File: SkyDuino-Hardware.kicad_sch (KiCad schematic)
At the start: 45 parts, among them J1 24V, J2 BT, J4 Drum, J5 Exhaust, J6 Cooling, J7 Cooling, J8 NTC, K1 RT314A24, Q1 DMN6075S, Q2 DMN6075S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

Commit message: Add Config field and exclude TH components from assembly
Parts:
- ACL1, ACN1, C1, C5, HEAT1, HEAT2, J1, J4, J5, J6, J7, K1, U6: Config (none) -> -jlcpcb
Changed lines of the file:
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@@
 			)
 		)
+		(property "Config" "-jlcpcb"
+			(at 20.32 77.47 0)
+			(effects
+				(font
+					(size 1.27 1.27)
+				)
+				(hide yes)
+			)
+		)
 		(pin "1"
 		)
@@
 			)
 		)
+		(property "Config" "-jlcpcb"
+			(at 227.33 68.58 0)
+			(effects
+				(font
+					(size 1.27 1.27)
+				)
+				(hide yes)
+			)
+		)
 		(pin "2"
 		)
@@
 			)
 		)
+		(property "Config" "-jlcpcb"
+			(at 245.11 93.98 0)
+			(effects
+				(font
+					(size 1.27 1.27)
+				)
+				(hide yes)
+			)
+		)
 		(pin "12"
 		)
@@
 			)
 		)
+		(property "Config" "-jlcpcb"
+			(at 274.32 86.36 0)
+			(effects
+				(font
+					(size 1.27 1.27)
+				)
+				(hide yes)
+			)
+		)
 		(pin "1"
 		)
@@
 			)
 		)
+		(property "Config" "-jlcpcb"
+			(at 64.77 77.47 0)
+			(effects
+				(font
+					(size 1.27 1.27)
+				)
+				(hide yes)
+			)
+		)
 		(pin "1"
 		)
@@
 			)
 		)
+		(property "Config" "-jlcpcb"
+			(at 274.32 71.12 0)
+			(effects
+				(font
+					(size 1.27 1.27)
+				)
+				(hide yes)
+			)
+		)
 		(pin "1"
 		)
@@
 			)
 		)
+		(property "Config" "-jlcpcb"
+			(at 274.32 66.04 0)
+			(effects
+				(font
+					(size 1.27 1.27)
+				)
+				(hide yes)
+			)
+		)
 		(pin "1"
 		)
@@
 			)
 		)
+		(property "Config" "-jlcpcb"
+			(at 24.13 27.94 0)
+			(effects
+				(font
+					(size 1.27 1.27)
+				)
+				(hide yes)
+			)
+		)
 		(pin "3"
 		)
@@
 			)
 		)
+		(property "Config" "-jlcpcb"
+			(at 36.83 77.47 0)
+			(effects
+				(font
+					(size 1.27 1.27)
+				)
+				(hide yes)
+			)
+		)
 		(pin "1"
 		)
@@
 			)
 		)
+		(property "Config" "-jlcpcb"
+			(at 52.07 77.47 0)
+			(effects
+				(font
+					(size 1.27 1.27)
+				)
+				(hide yes)
+			)
+		)
 		(pin "1"
 		)
@@
 			)
 		)
+		(property "Config" "-jlcpcb"
+			(at 45.72 30.48 0)
+			(effects
+				(font
+					(size 1.27 1.27)
+				)
+				(hide yes)
+			)
+		)
 		(pin "2"
 		)
@@
 			)
 		)
+		(property "Config" "-jlcpcb"
+			(at 121.92 41.91 0)
+			(effects
+				(font
+					(size 1.27 1.27)
+				)
+				(hide yes)
+			)
+		)
 		(pin "2"
 		)
@@
 			(at 274.32 81.28 0)
 			(effects
+				(font
+					(size 1.27 1.27)
+				)
+				(hide yes)
+			)
+		)
+		(property "Config" "-jlcpcb"
+			(at 274.32 81.28 0)
+			(effects

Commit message: Update LCSC field
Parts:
- C2, C9: LCSC (none) -> C377773
- C3, C6, C8: LCSC (none) -> C49678
- C4: LCSC (none) -> C45783
- C7: LCSC (none) -> C1710
- D1, D2, D4: LCSC (none) -> C14996
- J2, J8: Config (none) -> -jlcpcb
- L1: LCSC (none) -> C19947604; LCSC Orig Part (none) -> C19947604
- Q1, Q2, Q3: LCSC (none) -> C155242
- R1: LCSC (none) -> C706252
- R10, R21, R22, R5, R7, R8: LCSC (none) -> C17414
- R2: LCSC (none) -> C17560
- R20, R4, R6: LCSC (none) -> C17408
- R3: LCSC (none) -> C17633
- U1: LCSC (none) -> C5219371; Mouser pn 595-LV3842XFDBVR -> (none)
- U2: LCSC (none) -> C843273
- U3: LCSC (none) -> C52028
- U5: LCSC (none) -> C75864
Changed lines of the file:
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@@
 			)
 		)
-		(property "LCSC" ""
+		(property "LCSC" "C17414"
 			(at 96.52 182.88 0)
 			(effects
@@
 			)
 		)
-		(property "LCSC" ""
+		(property "LCSC" "C75864"
 			(at 36.83 104.14 0)
 			(effects
@@
 			)
 		)
-		(property "LCSC" ""
+		(property "LCSC" "C17408"
 			(at 102.87 134.62 0)
 			(effects
@@
 			)
 		)
-		(property "LCSC" ""
+		(property "LCSC" "C17414"
 			(at 209.55 72.39 0)
 			(effects
@@
 			)
 		)
-		(property "LCSC" ""
+		(property "LCSC" "C706252"
 			(at 100.33 35.56 0)
 			(effects
@@
 			)
 		)
-		(property "LCSC" ""
+		(property "LCSC" "C49678"
 			(at 82.55 27.94 0)
 			(effects
@@
 			)
 		)
-		(property "LCSC" ""
+		(property "LCSC" "C17560"
 			(at 100.33 45.72 0)
 			(effects
@@
 			)
 		)
-		(property "LCSC" ""
+		(property "LCSC" "C14996"
 			(at 86.36 166.37 0)
 			(effects
@@
 			)
 		)
-		(property "LCSC" ""
+		(property "LCSC" "C5219371"
 			(at 68.58 30.48 0)
 			(effects
@@
 			)
 		)
-		(property "Mouser pn" "595-LV3842XFDBVR"
+		(property "Mouser pn" ""
 			(at 68.58 29.21 0)
 			(effects
@@
 			)
 		)
-		(property "LCSC" ""
+		(property "LCSC" "C17633"
 			(at 24.13 115.57 0)
 			(effects
@@
 			)
 		)
-		(property "LCSC" ""
+		(property "LCSC" "C1710"
 			(at 220.98 36.83 0)
 			(effects
@@
 			)
 		)
-		(property "LCSC" ""
+		(property "LCSC" "C17414"
 			(at 96.52 97.79 0)
 			(effects
@@
 			)
 		)
-		(property "LCSC" ""
+		(property "LCSC" "C17408"
 			(at 102.87 179.07 0)
 			(effects
@@
 			)
 		)
-		(property "LCSC" ""
+		(property "LCSC" "C14996"
 			(at 86.36 121.92 0)
 			(effects
@@
 			)
 		)
-		(property "LCSC" ""
+		(property "LCSC" "C49678"
 			(at 265.43 29.21 0)
 			(effects
@@
 			)
 		)
-		(property "LCSC" ""
+		(property "LCSC" "C17414"
 			(at 52.07 110.49 0)
 			(effects
@@
 			)
 		)
+		(property "Config" "-jlcpcb"
+			(at 212.09 35.56 0)
+			(effects
+				(font
+					(size 1.27 1.27)
+				)
+				(hide yes)
+			)
+		)
 		(pin "1"
 		)
@@
 			)
 		)
-		(property "LCSC" ""
+		(property "LCSC" "C377773"
 			(at 52.07 30.48 0)
 			(effects
@@
 			)
 		)
-		(property "LCSC" ""
+		(property "LCSC" "C17414"
 			(at 96.52 138.43 0)
 			(effects
@@
 			)
 		)
-		(property "LCSC" ""
+		(property "LCSC" "C14996"
 			(at 86.36 81.28 0)
 			(effects
@@
 			)
 		)
+		(property "Config" "-jlcpcb"
+			(at 38.1 180.34 0)
+			(effects
+				(font
+					(size 1.27 1.27)
+				)
+				(hide yes)
+			)
+		)
 		(pin "1"
 		)
@@
 			)
 		)
-		(property "LCSC" ""
+		(property "LCSC" "C19947604"
 			(at 93.98 30.48 0)
 			(effects
@@
 			)
 		)
+		(property "Config" ""
+			(at 93.98 30.48 0)
+			(effects
+				(font
+					(size 1.27 1.27)
+				)
+				(hide yes)
+			)
+		)
+		(property "LCSC Orig Part" "C19947604"
+			(at 93.98 30.48 90)
+			(effects
+				(font
+					(size 1.27 1.27)
+				)
+				(hide yes)
+			)
+		)
 		(pin "2"
 		)
@@
 			)
 		)
-		(property "LCSC" ""
+		(property "LCSC" "C377773"
 			(at 64.77 96.52 0)
 			(effects
@@
 			)
 		)
-		(property "LCSC" ""
+		(property "LCSC" "C52028"
 			(at 240.03 36.83 0)
 			(effects
@@
 			)
 		)
-		(property "LCSC" ""
+		(property "LCSC" "C155242"
 			(at 88.9 134.62 0)
 			(effects
@@
 			)
 		)
-		(property "LCSC" ""
+		(property "LCSC" "C155242"
 			(at 88.9 93.98 0)
 			(effects
@@
 			)
 		)
-		(property "LCSC" ""
+		(property "LCSC" "C17414"
 			(at 27.94 173.99 0)
 			(effects
@@
 			)
 		)
-		(property "LCSC" ""
+		(property "LCSC" "C45783"
 			(at 110.49 41.91 0)
 			(effects
@@
 			)
 		)
-		(property "LCSC" ""
+		(property "LCSC" "C49678"
 			(at 179.07 41.91 0)
 			(effects
@@
 			)
 		)
-		(property "LCSC" ""
+		(property "LCSC" "C17408"
 			(at 102.87 93.98 0)
 			(effects
@@
 			)
 		)
-		(property "LCSC" ""
+		(property "LCSC" "C155242"
 			(at 88.9 179.07 0)
 			(effects
@@
 			)
 		)
-		(property "LCSC" ""
+		(property "LCSC" "C843273"
 			(at 161.29 33.02 0)
 			(effects

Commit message: Add JLC rotation offsets
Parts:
- U1: JLCRotOffset (none) -> -90
- U2: JLCRotOffset (none) -> 180
- U5: JLCRotOffset (none) -> 90
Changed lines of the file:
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@@
 			)
 		)
+		(property "Config" ""
+			(at 36.83 104.14 0)
+			(effects
+				(font
+					(size 1.27 1.27)
+				)
+				(hide yes)
+			)
+		)
+		(property "JLCRotOffset" "90"
+			(at 36.83 104.14 0)
+			(effects
+				(font
+					(size 1.27 1.27)
+				)
+				(hide yes)
+			)
+		)
 		(pin "4"
 		)
@@
 			)
 		)
-		(property "Mouser pn" ""
-			(at 68.58 29.21 0)
+		(property "Config" ""
+			(at 68.58 30.48 0)
+			(effects
+				(font
+					(size 1.27 1.27)
+				)
+				(hide yes)
+			)
+		)
+		(property "JLCRotOffset" "-90"
+			(at 68.58 30.48 0)
 			(effects
 				(font
@@
 			(at 161.29 33.02 0)
 			(effects
+				(font
+					(size 1.27 1.27)
+				)
+				(hide yes)
+			)
+		)
+		(property "Config" ""
+			(at 161.29 33.02 0)
+			(effects
+				(font
+					(size 1.27 1.27)
+				)
+				(hide yes)
+			)
+		)
+		(property "JLCRotOffset" "180"
+			(at 161.29 33.02 0)
+			(effects

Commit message: Rotate U5 in correct direction
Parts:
- U5: JLCRotOffset 90 -> -90
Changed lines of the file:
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@@
 			)
 		)
-		(property "JLCRotOffset" "90"
+		(property "JLCRotOffset" "-90"
 			(at 36.83 104.14 0)
 			(effects

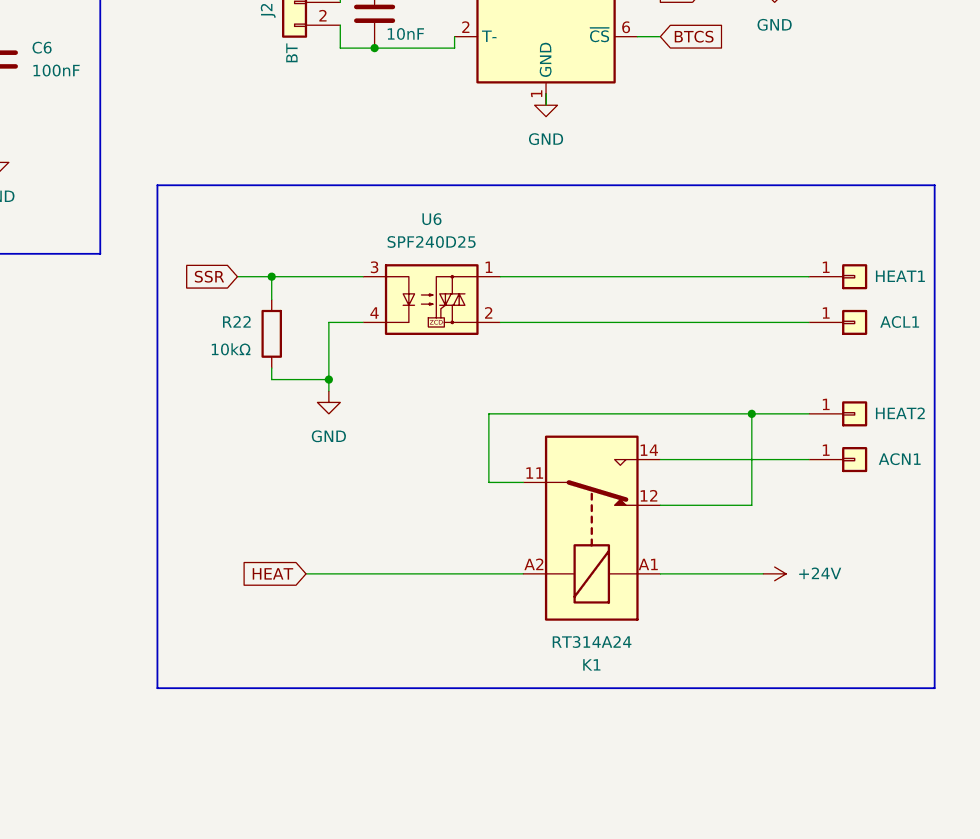
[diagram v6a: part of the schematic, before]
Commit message: Reposition SSR to fit into vented enclosure
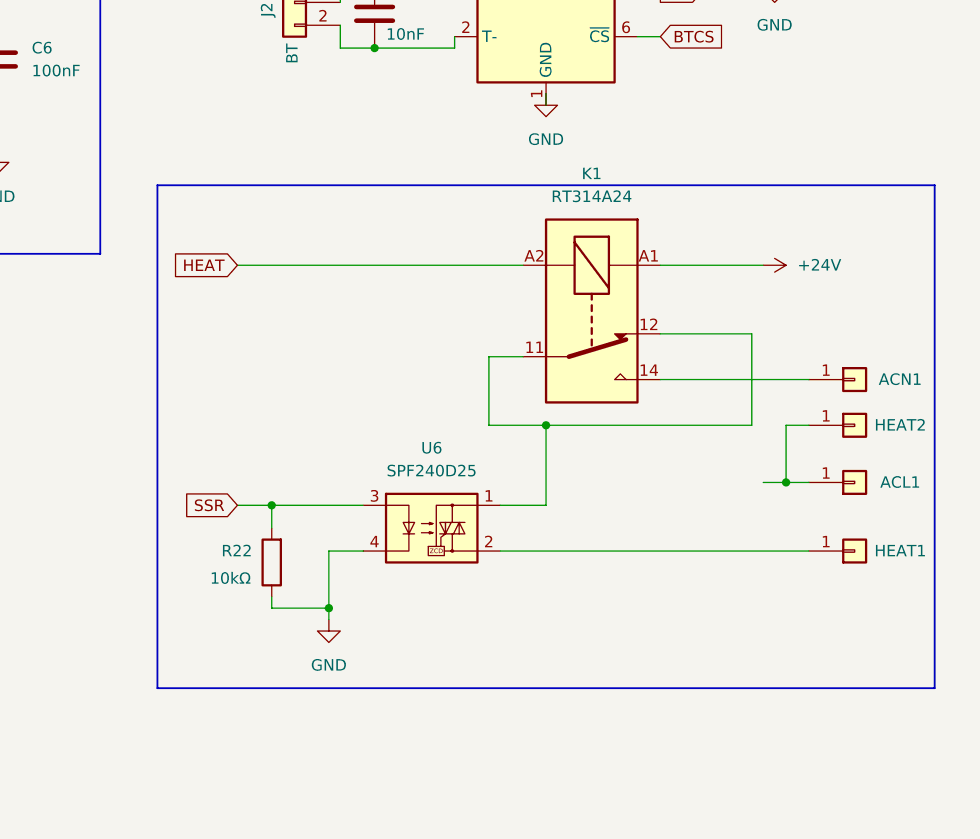
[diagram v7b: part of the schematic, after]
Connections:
- net at U6.1: now also K1.11, K1.12; no longer HEAT1.1 (Pin_1)
- net at U6.2: now also HEAT1.1 (Pin_1); no longer ACL1.1 (Pin_1)
- new net: ACL1.1 (Pin_1), HEAT2.1 (Pin_1)
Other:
- moved on the sheet: ACL1, ACN1, HEAT1, HEAT2, K1, R22, U6

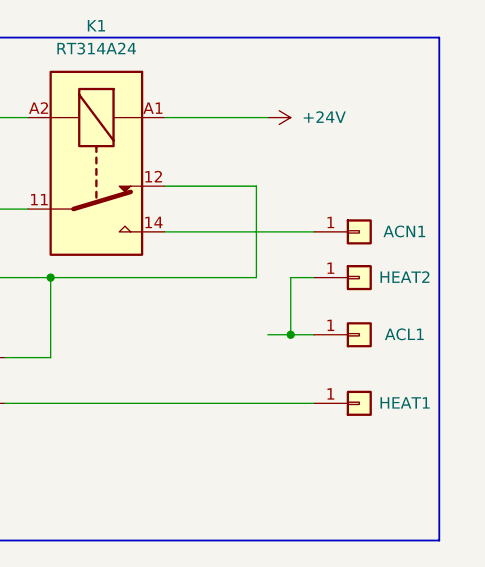
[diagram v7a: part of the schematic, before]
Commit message: Swap AC-Live and AC-Neutral on PCB (#9)
Swap Live with Neutral on PCB, so the live is controlled by the Relay.
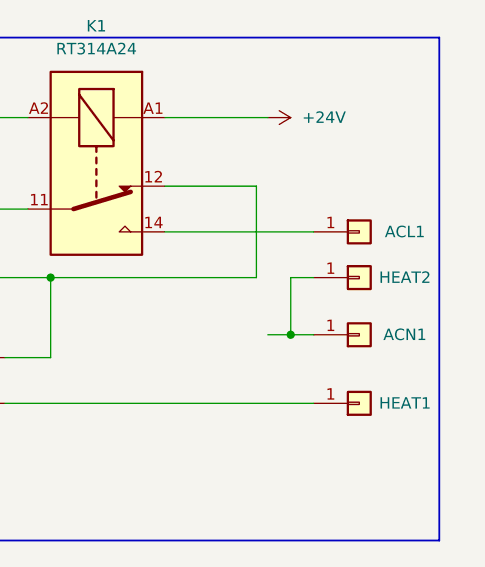
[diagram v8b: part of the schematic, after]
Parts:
- renumbered ACN1 to ACL1, ACL1 to ACN1
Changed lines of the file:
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@@
 		(on_board yes)
 		(dnp no)
-		(property "Reference" "ACN1"
+		(property "Reference" "ACL1"
 			(at 279.4 77.47 0)
 			(effects
@@
 			(project "SkyDuino-Hardware"
 				(path "/a6671232-96de-4e23-ad68-f9378c1c0159"
-					(reference "ACN1")
+					(reference "ACL1")
 					(unit 1)
 				)
@@
 		(on_board yes)
 		(dnp no)
-		(property "Reference" "ACL1"
+		(property "Reference" "ACN1"
 			(at 279.4 88.9 0)
 			(effects
@@
 			(project "SkyDuino-Hardware"
 				(path "/a6671232-96de-4e23-ad68-f9378c1c0159"
-					(reference "ACL1")
-					(unit 1)
-				)
+					(reference "ACN1")
+					(unit 1)
+				)
